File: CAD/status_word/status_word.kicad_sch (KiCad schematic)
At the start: 45 parts, among them J1 Conn_01x26_Pin, U1 74HC161, U2 74HC109, U3 74HC157, U4 74HC157, U5 74HC245, U6 74HC02

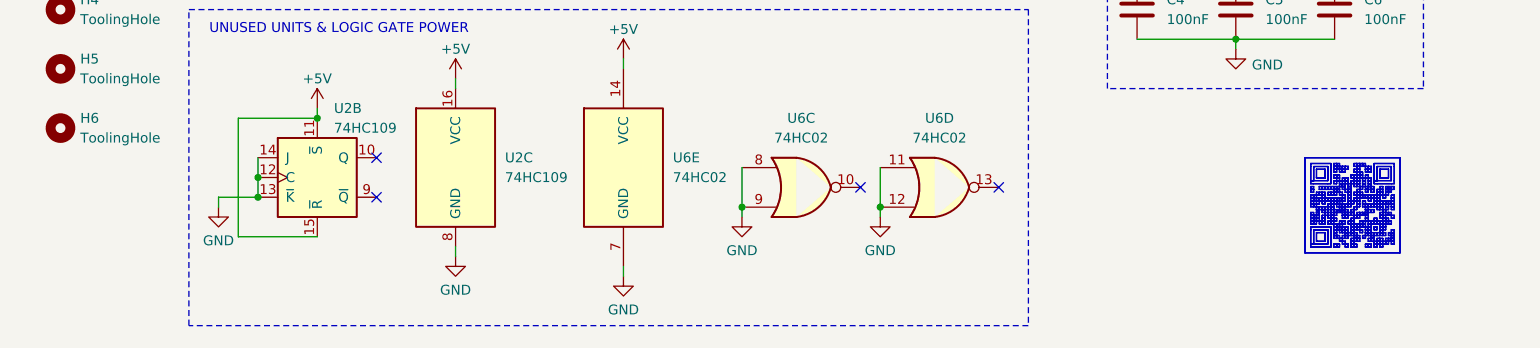
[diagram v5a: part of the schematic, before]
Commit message: CLK test point, CC-BY-NC-SA
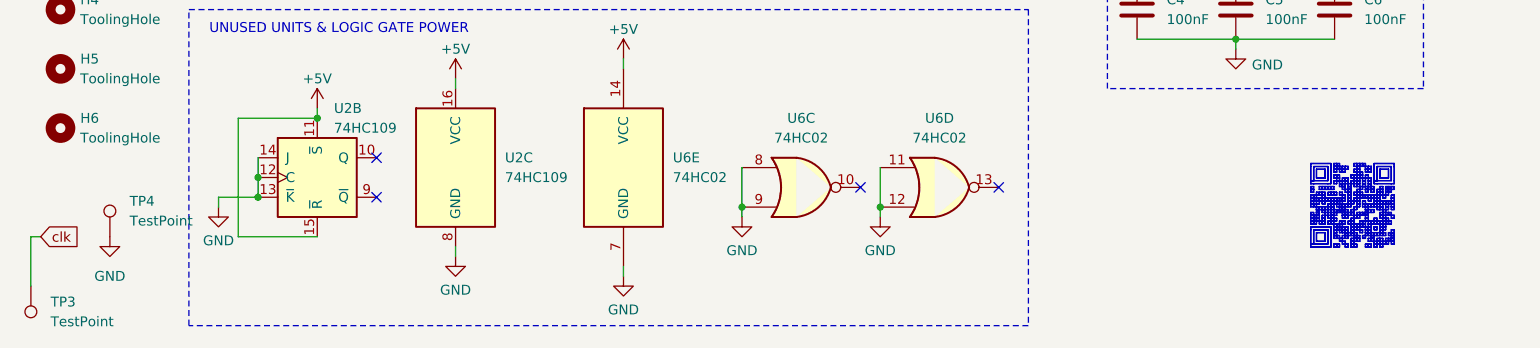
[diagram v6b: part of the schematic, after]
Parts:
- added TP3, TP4: TestPoint, TestPoint:TestPoint_THTPad_D1.0mm_Drill0.5mm, symbol Connector:TestPoint
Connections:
- net GND: now also TP4.1
- net clk: now also TP3.1

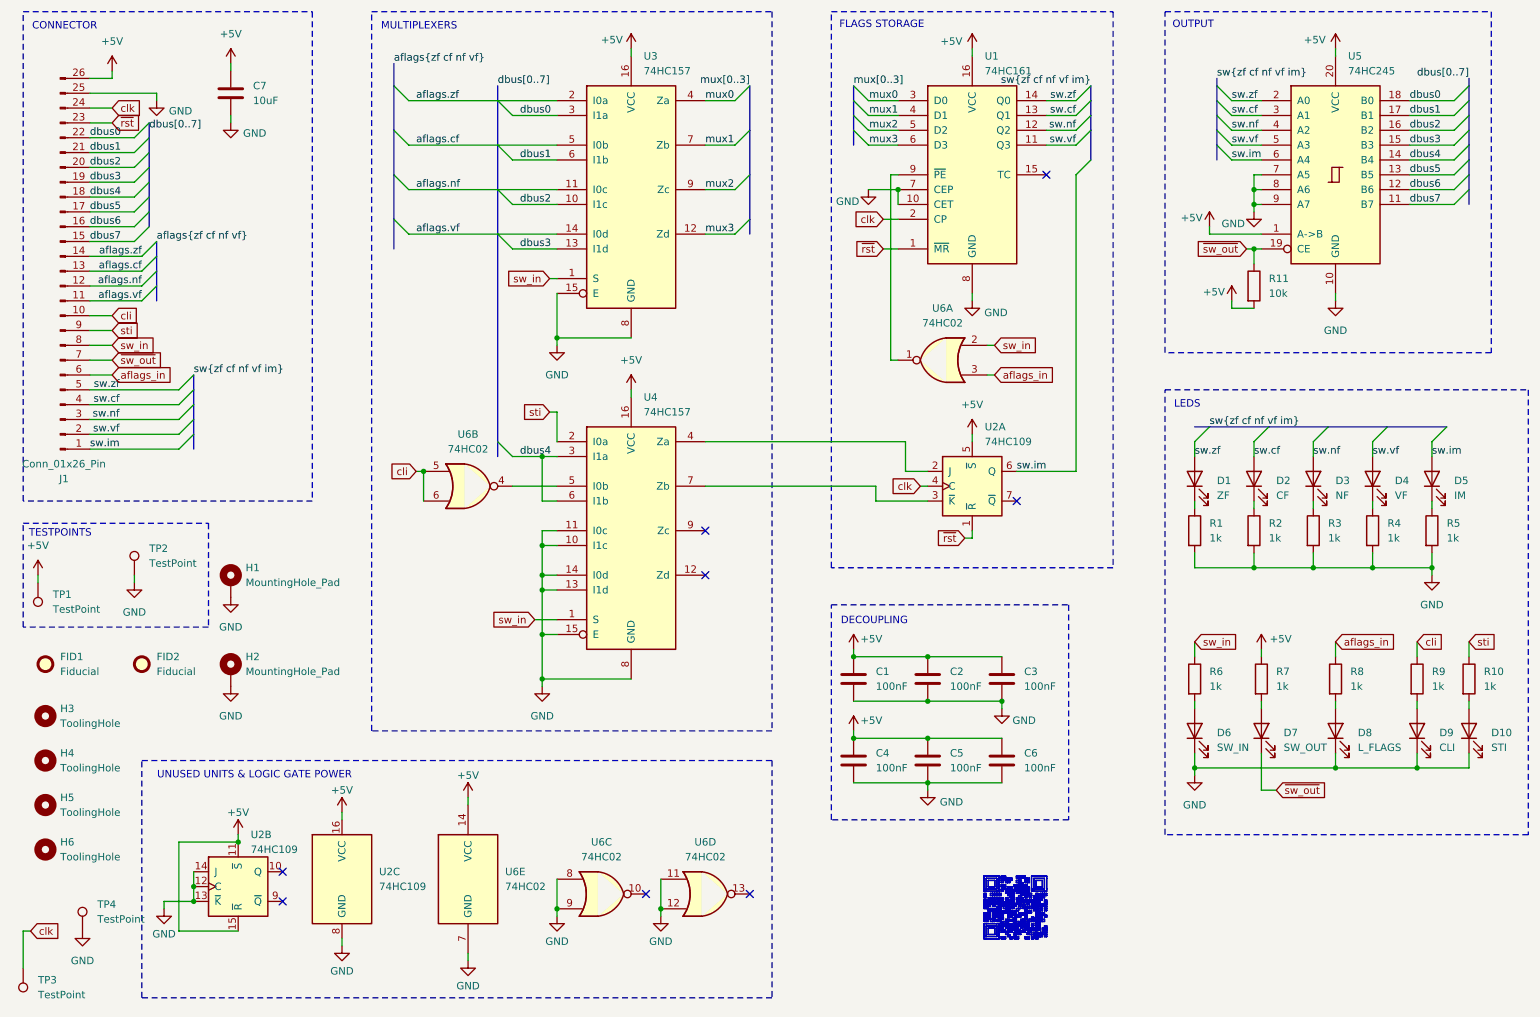
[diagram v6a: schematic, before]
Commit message: update SW, add footprints and 3D models to library
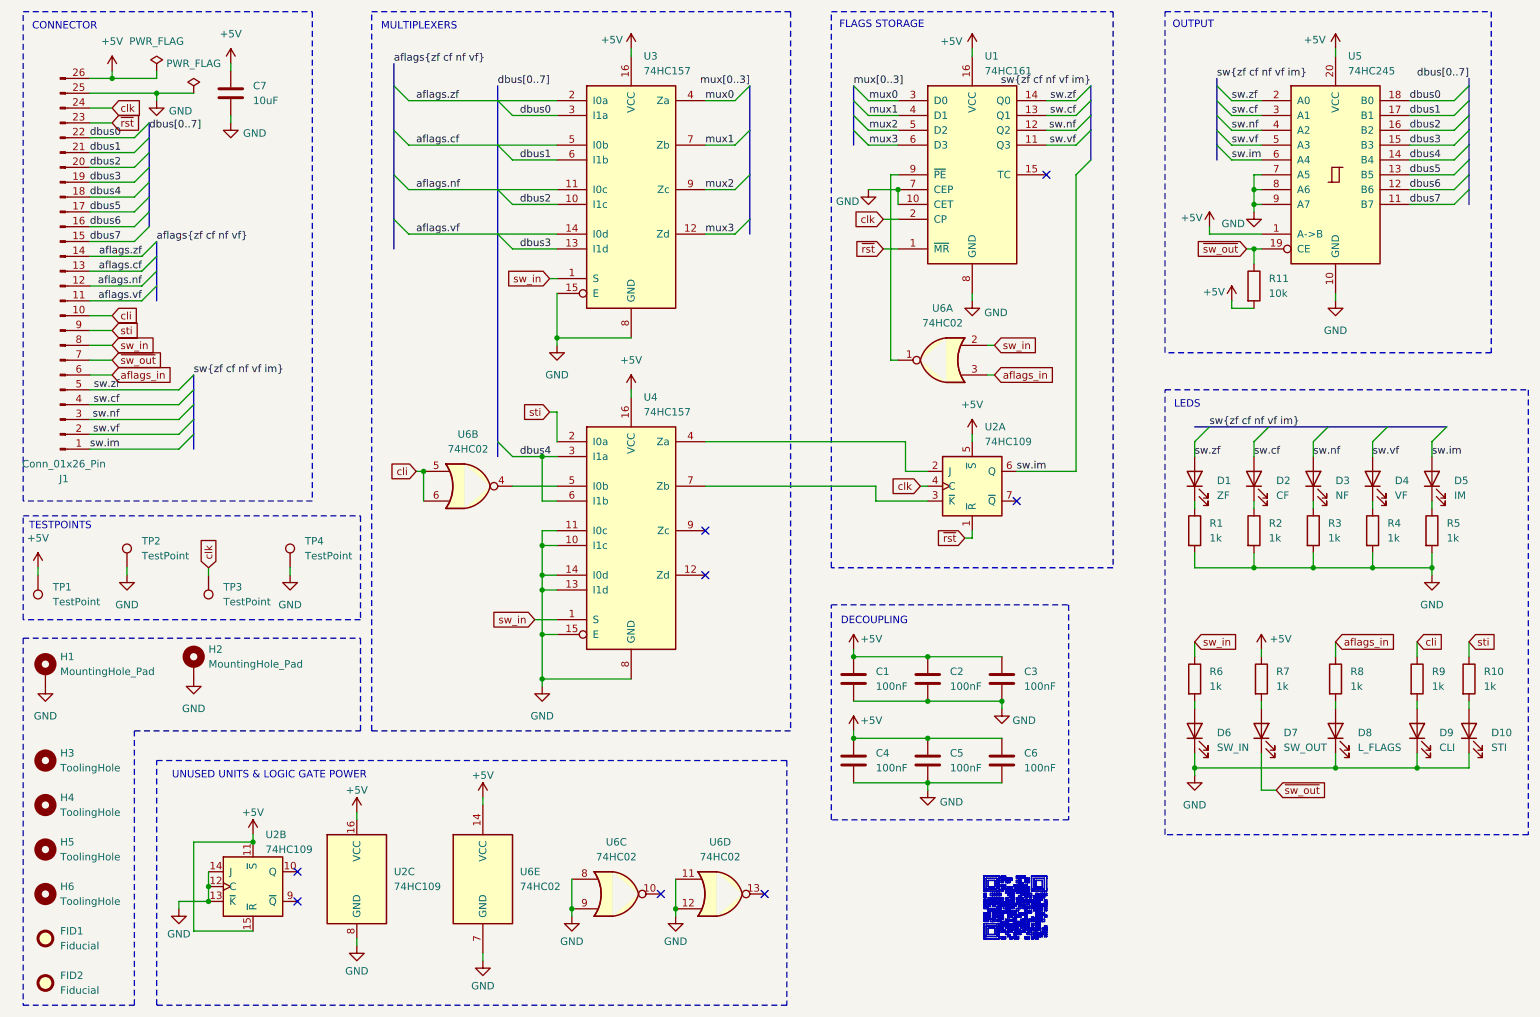
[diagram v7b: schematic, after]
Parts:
- U6: Details https://www.lcsc.com/product-detail/C253895.html -> https://www.lcsc.com/product-detail/C350559.html; LCSC C253895 -> C350559
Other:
- moved on the sheet: FID1, FID2, H1, H2, H3, H4, H5, H6, TP1, TP2, TP3, TP4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

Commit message: update SW, fix component rotations
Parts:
- C1, C2, C3, C4, C5, C6: LCSC (none) -> C28233
- C7: LCSC (none) -> C15850
- D1, D2, D3, D4, D5: LCSC (none) -> C84256
- D10, D7, D9: LCSC (none) -> C2296
- D6, D8: LCSC (none) -> C2297
- J1: LCSC (none) -> C2894993
- R1, R10, R2, R3, R4, R5, R6, R7, R8, R9: LCSC (none) -> C17513
- R11: LCSC (none) -> C17414
- TP1, TP2, TP3, TP4: now left out of the parts list
